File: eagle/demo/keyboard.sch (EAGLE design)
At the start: 9 parts, among them X1 MALE_2X1-T-VERTICAL, X2 CLAMP_1X2-T-2.5MM

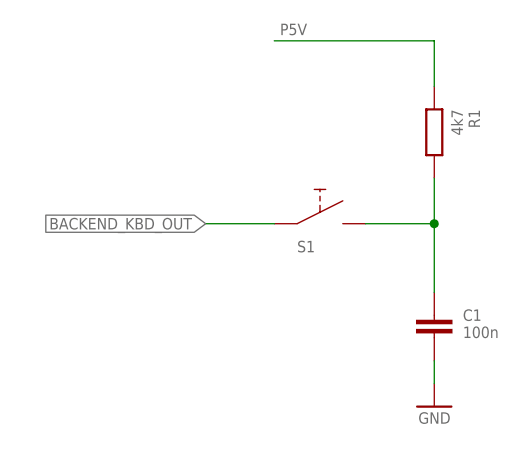
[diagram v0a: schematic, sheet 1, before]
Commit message: fixed prefixes
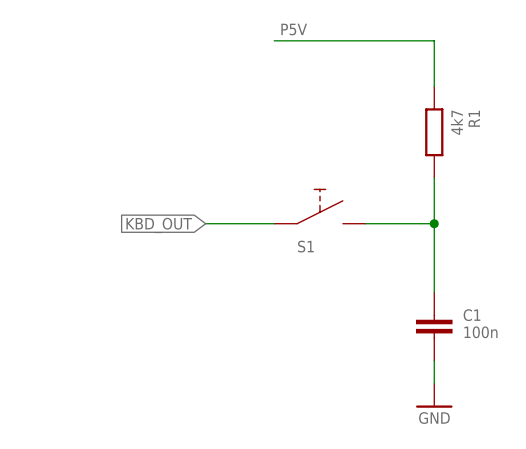
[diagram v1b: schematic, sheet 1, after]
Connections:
- net BACKEND_KBD_OUT renamed KBD_OUT
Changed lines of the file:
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@@
 </segment>
 </net>
-<net name="BACKEND_KBD_OUT" class="0">
+<net name="KBD_OUT" class="0">
 <segment>
 <pinref part="S1" gate="G$1" pin="A1"/>
@@
 </segment>
 </net>
-<net name="BACKEND_KBD_OUT" class="0">
+<net name="KBD_OUT" class="0">
 <segment>
 <pinref part="X1" gate="G$1" pin="2"/>
